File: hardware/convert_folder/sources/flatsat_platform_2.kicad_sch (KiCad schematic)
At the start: 0 parts

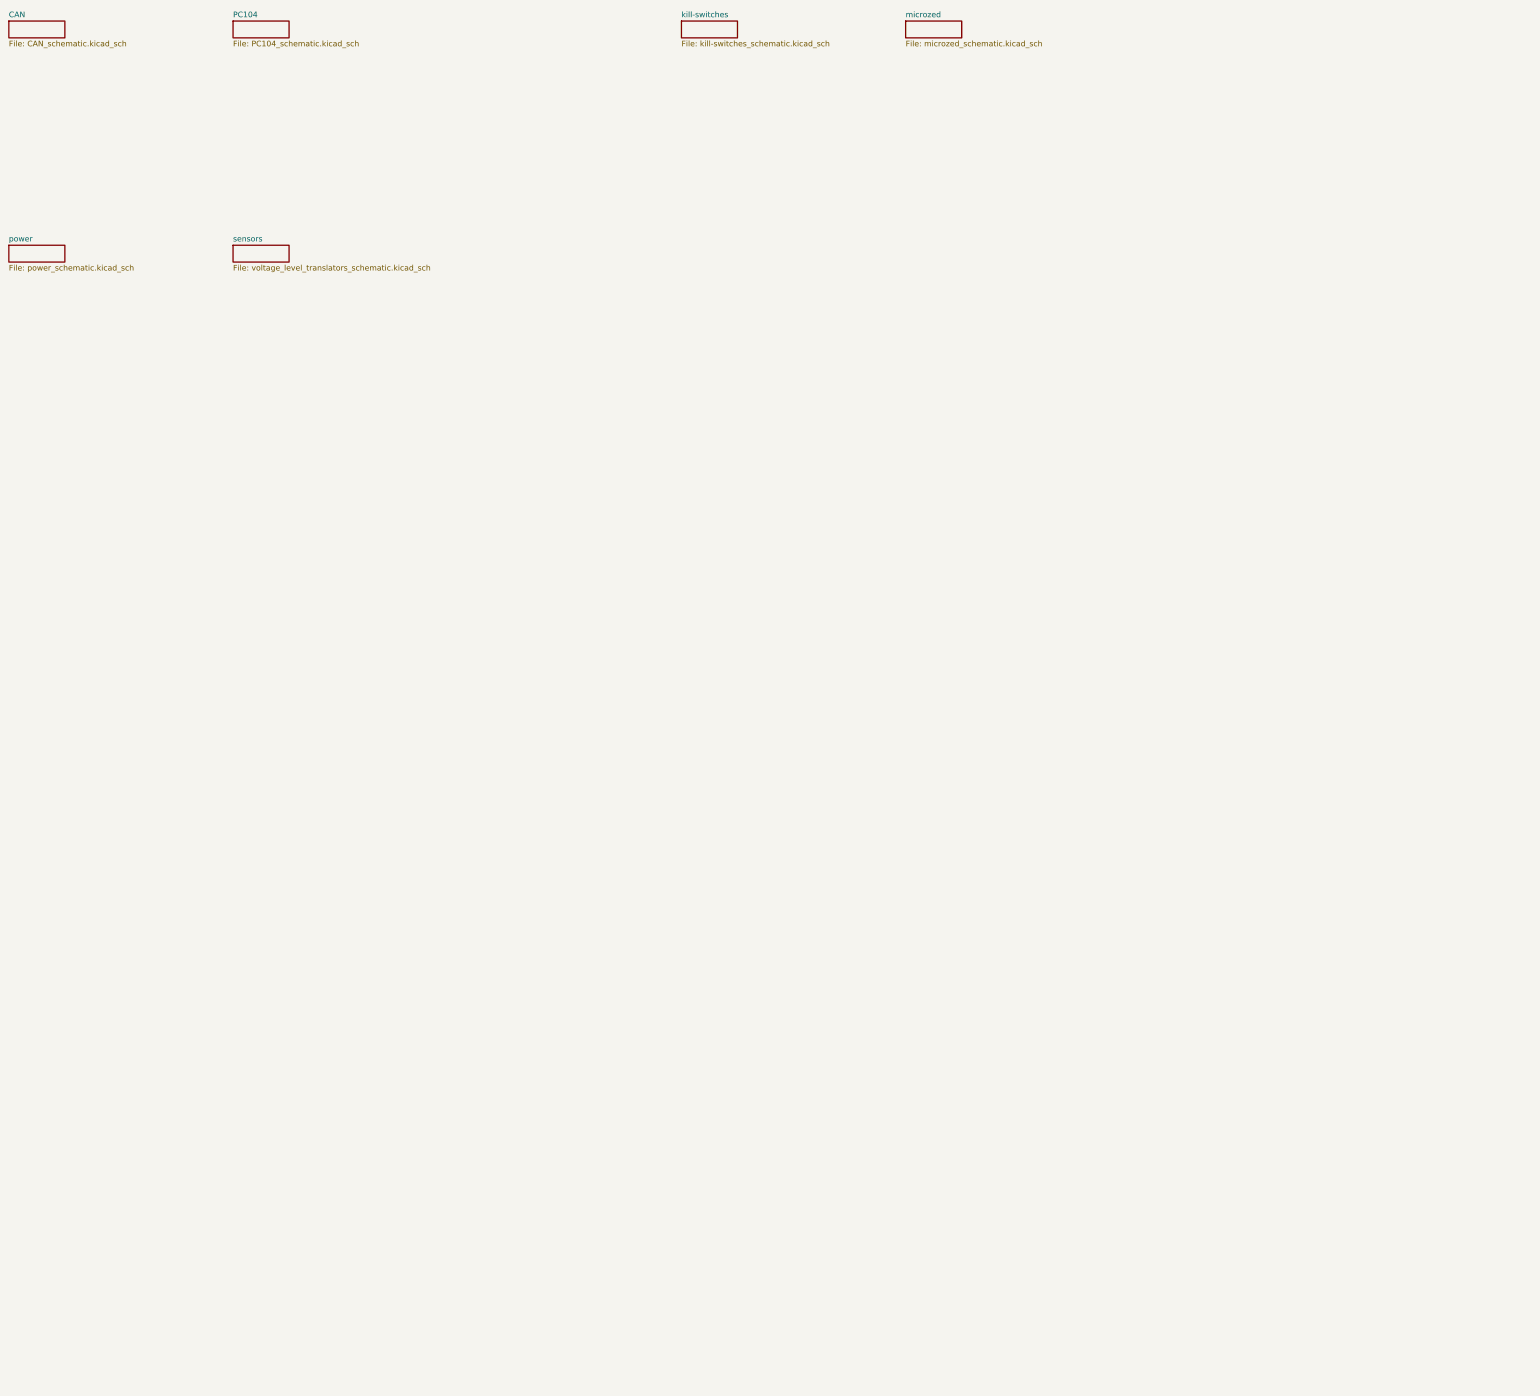
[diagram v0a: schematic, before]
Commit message: fix: fix a lot of connections between blocks. Many more to go...
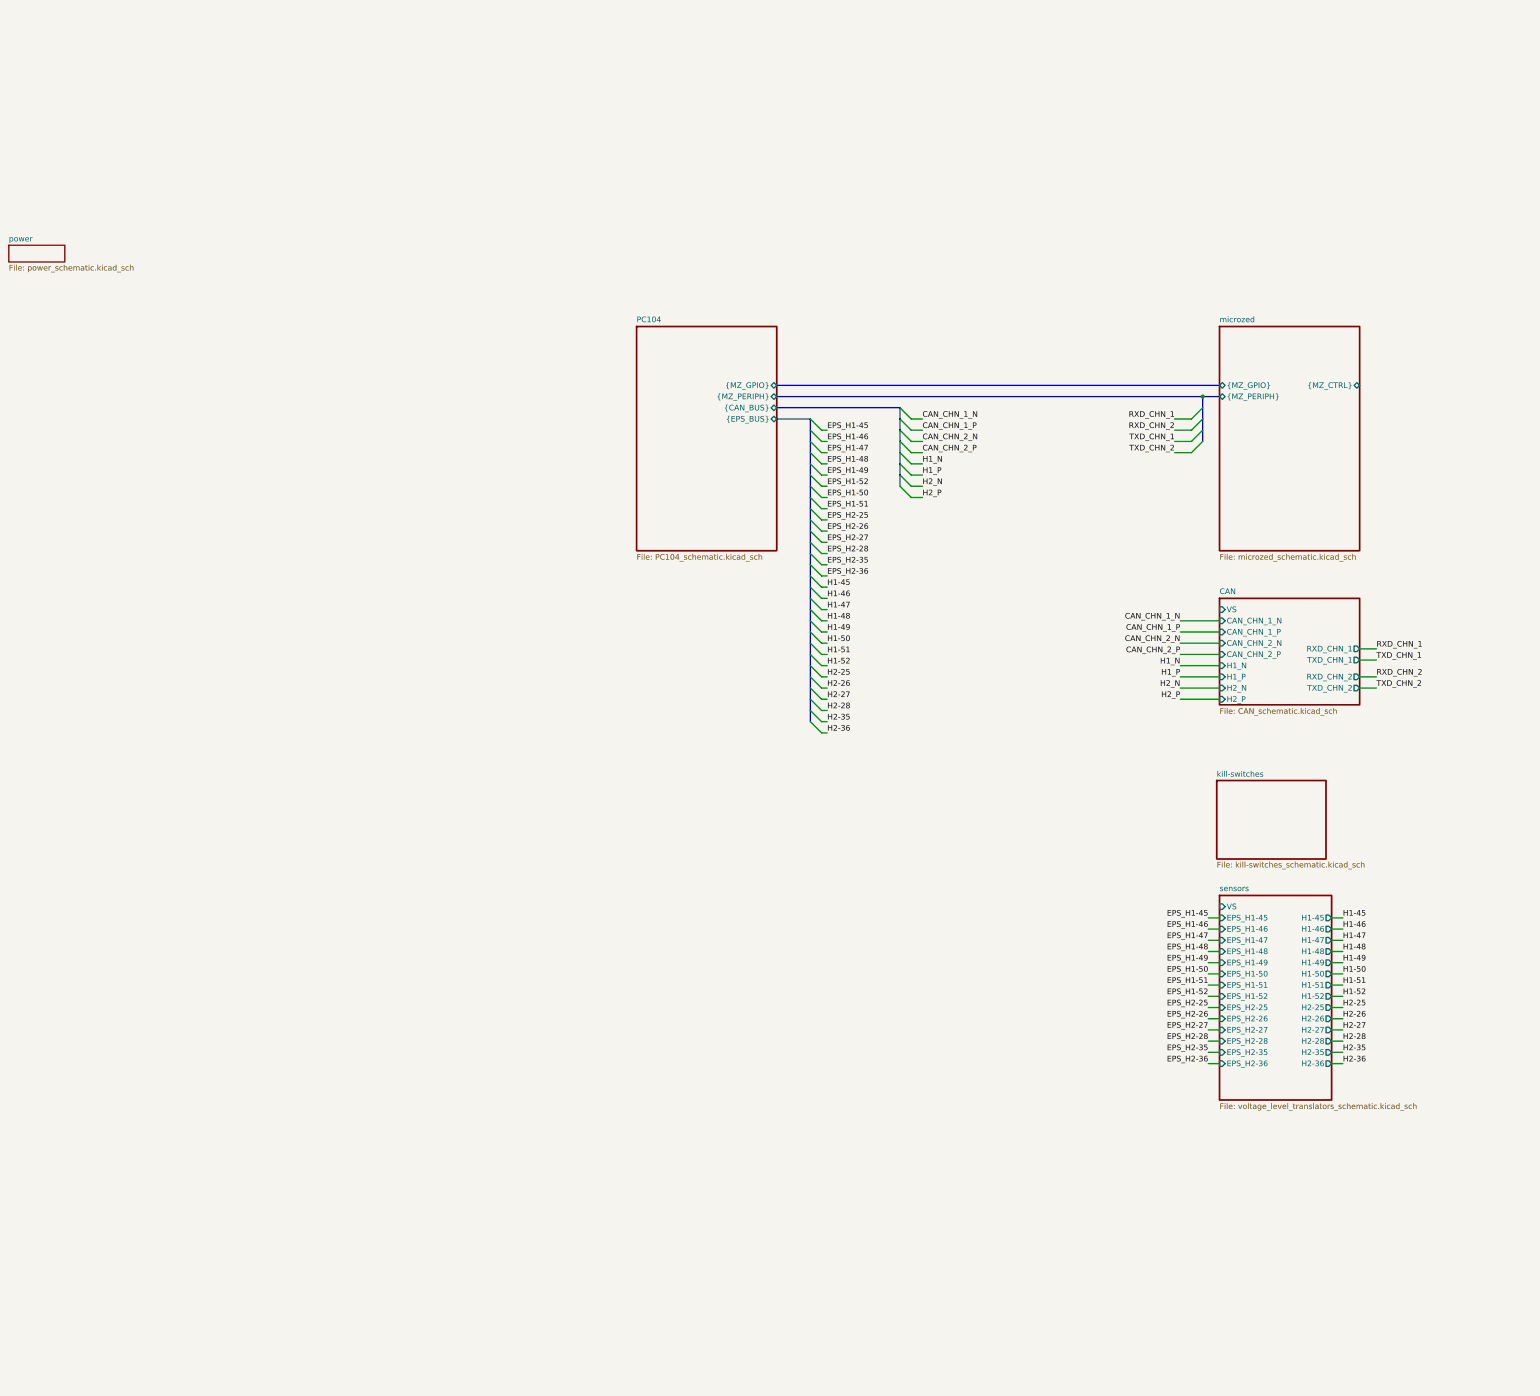
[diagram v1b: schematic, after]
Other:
- sheet CAN ports: added CAN_CHN_1_N, CAN_CHN_1_P, CAN_CHN_2_N, CAN_CHN_2_P, H1_N, H1_P, H2_N, H2_P, RXD_CHN_1, RXD_CHN_2, TXD_CHN_1, TXD_CHN_2, VS; removed none
- sheet PC104 ports: added {CAN_BUS}, {EPS_BUS}, {MZ_GPIO}, {MZ_PERIPH}; removed none
- sheet microzed ports: added {MZ_CTRL}, {MZ_GPIO}, {MZ_PERIPH}; removed none
- sheet sensors ports: added EPS_H1-45, EPS_H1-46, EPS_H1-47, EPS_H1-48, EPS_H1-49, EPS_H1-50, EPS_H1-51, EPS_H1-52, EPS_H2-25, EPS_H2-26, EPS_H2-27, EPS_H2-28, EPS_H2-35, EPS_H2-36, H1-45, H1-46, H1-47, H1-48, H1-49, H1-50, H1-51, H1-52, H2-25, H2-26, H2-27, H2-28, H2-35, H2-36, VS; removed none

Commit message: fix: convert 90% of the schematic (there are 21 warnings/errors to resolve)
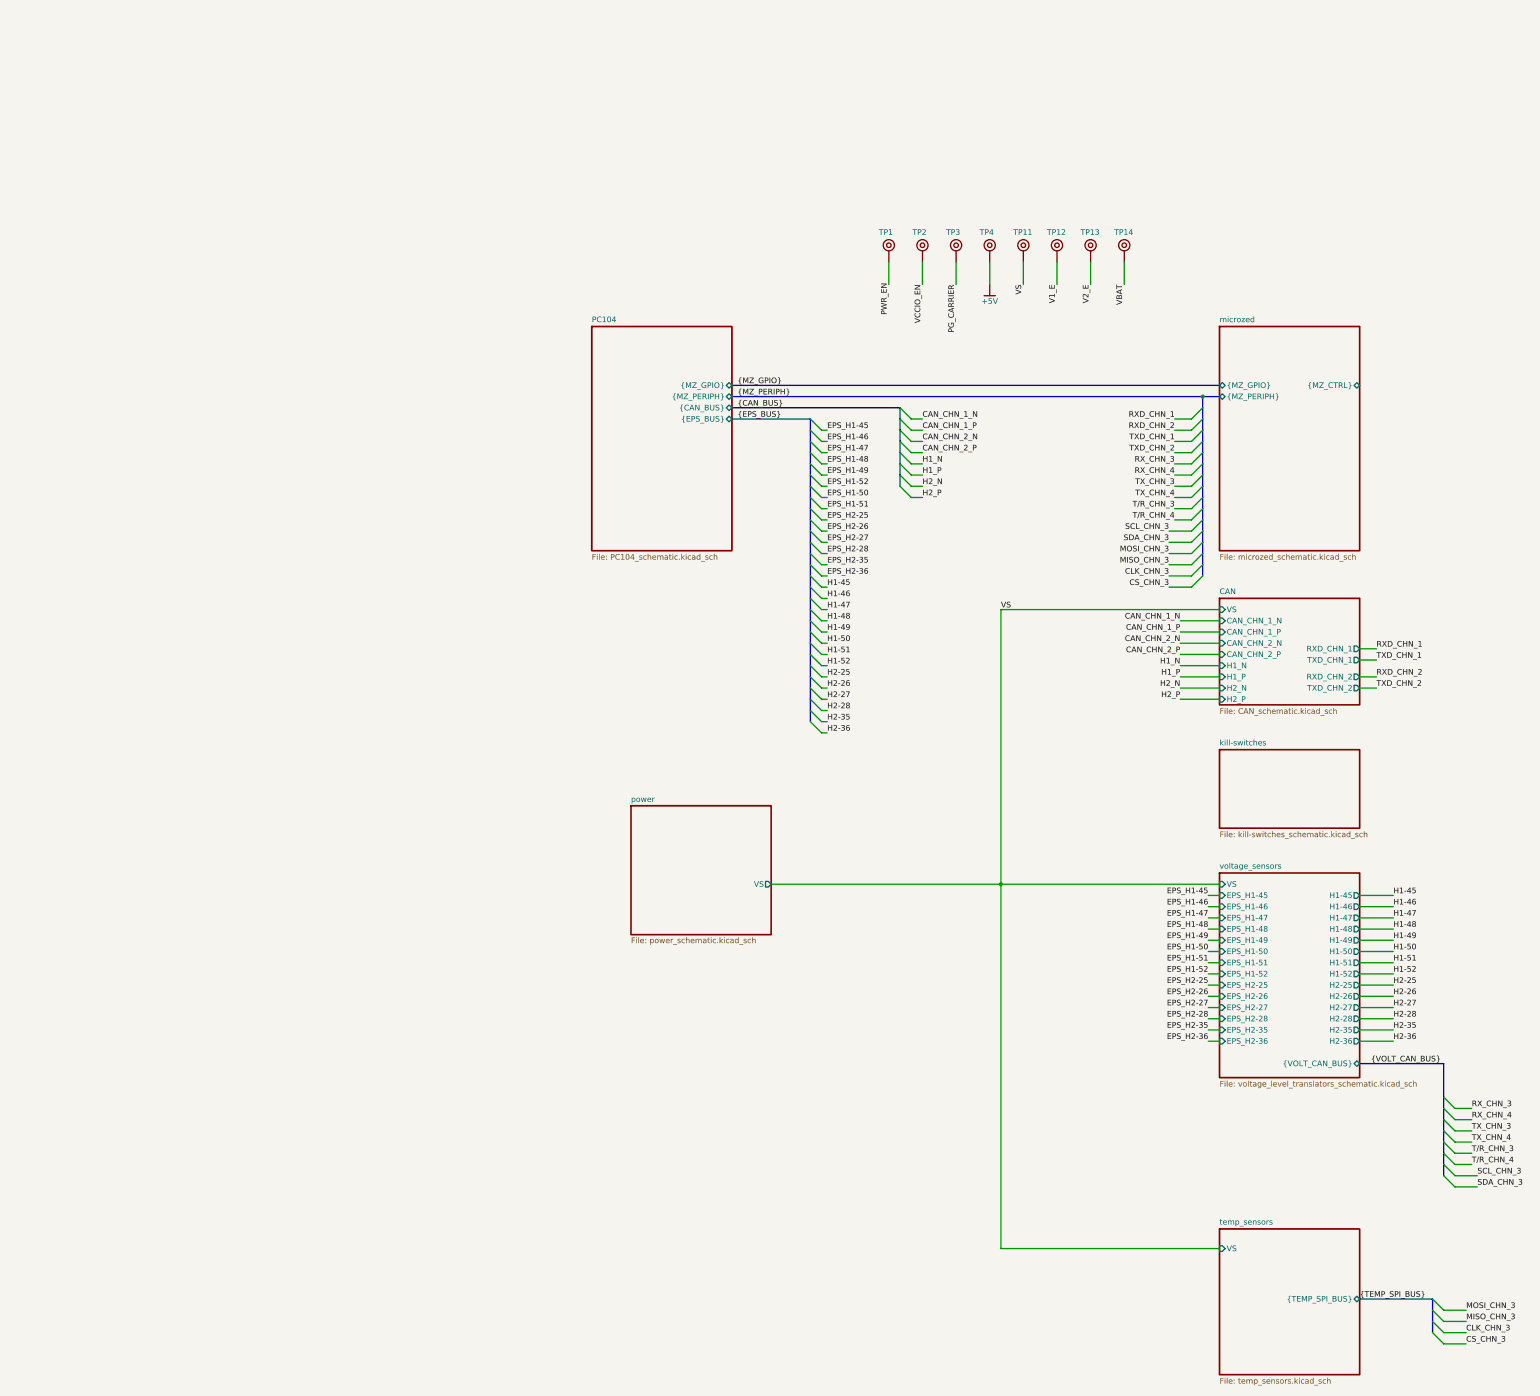
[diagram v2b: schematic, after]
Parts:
- added TP1, TP11, TP12, TP13, TP14, TP2, TP3, TP4: ~, altium_import:TEST POINT PTH, symbol altium_import:root_0_Test Point PTH_flatsat_platform_2.SchLib
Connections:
- new net +5V: TP4.1
- new net PG_CARRIER: TP3.1
- new net PWR_EN: TP1.1
- new net V1_E: TP12.1
- new net V2_E: TP13.1
- new net VBAT: TP14.1
- new net VCCIO_EN: TP2.1
- new net VS: TP11.1
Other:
- sheet sensors renamed voltage_sensors
- added sheet temp_sensors (temp_sensors.kicad_sch)
- sheet power ports: added VS; removed none
- sheet voltage_sensors ports: added {VOLT_CAN_BUS}; removed none

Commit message: fix: add more fixes to the power converters, add resets and other minor corrections
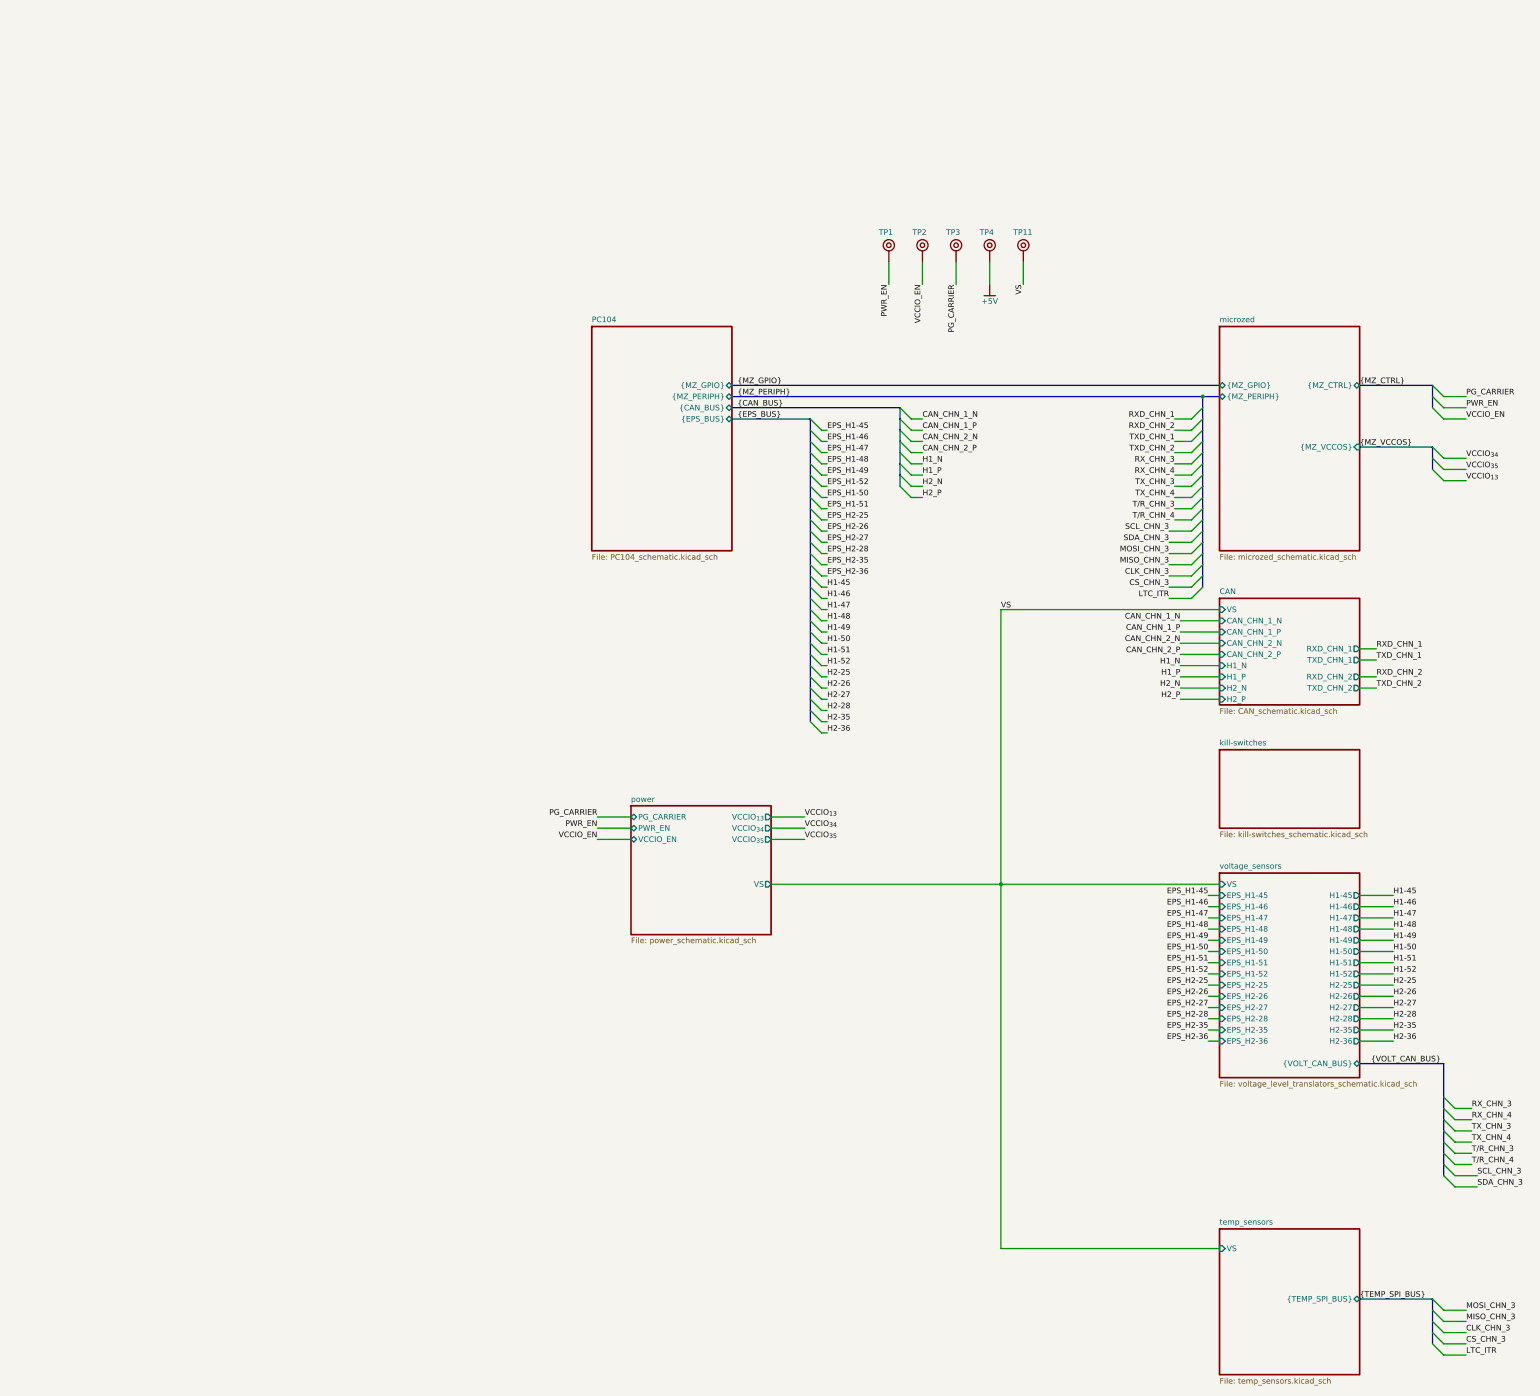
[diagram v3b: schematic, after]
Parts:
- removed TP12, TP13, TP14: ~, altium_import:TEST POINT PTH, symbol altium_import:root_0_Test Point PTH_flatsat_platform_2.SchLib
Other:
- sheet microzed ports: added {MZ_VCCOS}; removed none
- sheet power ports: added PG_CARRIER, PWR_EN, VCCIO_EN, VCCIO_{13}, VCCIO_{34}, VCCIO_{35}; removed none
